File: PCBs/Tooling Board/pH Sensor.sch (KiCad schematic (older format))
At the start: 28 parts

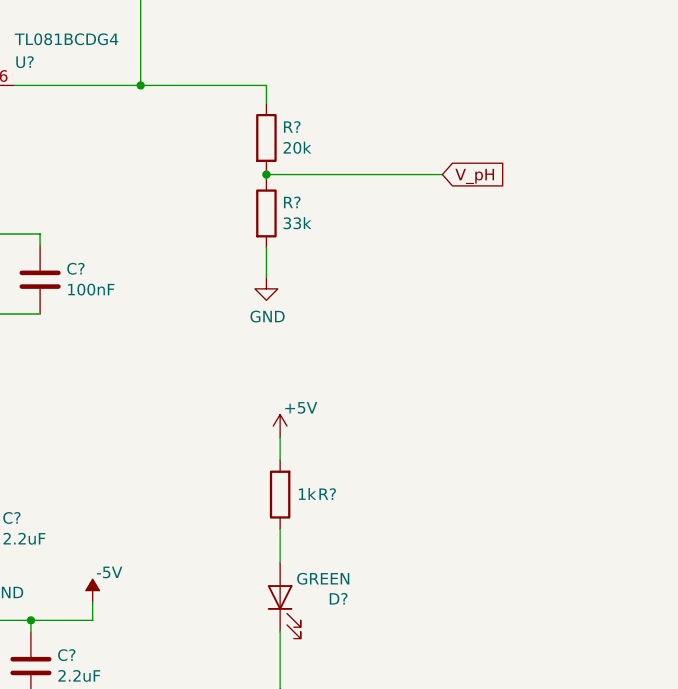
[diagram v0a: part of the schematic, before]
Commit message: Pins are Mapped
-This was really difficult and it may not work.
-We're gonna try it and see what works.
-If it fails the next PCB will use arduino atmega chips since the open source libraries exist for them
-Might do a combination of SAMD and atmega lol
-God damn chinese new year
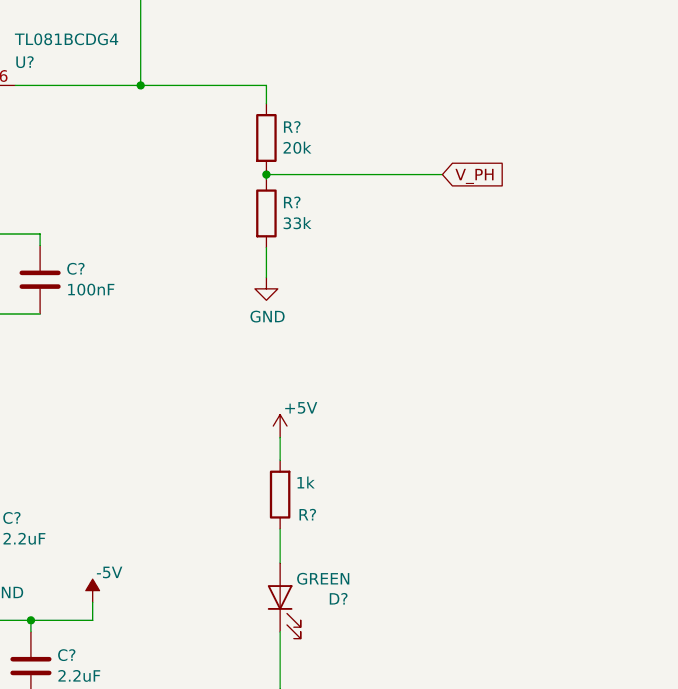
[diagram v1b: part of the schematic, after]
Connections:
- net V_pH renamed V_PH
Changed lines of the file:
@@
 EESchema Schematic File Version 4
-LIBS:Actuator Board-cache
+LIBS:Tooling Board-cache
 EELAYER 26 0
 EELAYER END
@@
 U 1 1 5BE3019B
 P 8510 4190
-F 0 "R?" H 8303 4190 50  0000 C CNN
-F 1 "1k" H 8394 4190 50  0000 C CNN
+F 0 "R?" H 8390 4280 50  0000 C CNN
+F 1 "1k" H 8400 4140 50  0000 C CNN
 F 2 "" V 8440 4190 50  0001 C CNN
 F 3 "~" H 8510 4190 50  0001 C CNN
@@
 	5980 1490 5980 1550
 Text GLabel 9220 2790 2    50   Input ~ 0
-V_pH
-$Comp
-L Device:R R?
+V_PH
+$Comp
+L Device:R R?

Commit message: Added Footprints
-Whoooo boy here we go
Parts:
- C801, C802, C803, C804, C805, C806, C807, C808, C809, C810, C811, C812, C813: renamed from C?; footprint (none) -> Capacitors_SMD:C_0805_HandSoldering
- D801: renamed from D?; footprint (none) -> LEDs:LED_0805_HandSoldering
- J801: renamed from J?; footprint (none) -> Junction Box:70553-02
- R801, R802, R803, R804, R805, R806, R807, R808, R809: renamed from R?; footprint (none) -> Resistors_SMD:R_0805_HandSoldering
- RV801: renamed from RV?; footprint (none) -> Potentiometers:Potentiometer_Trimmer_Bourns_3269W
- U801, U803: renamed from U?; footprint (none) -> SMD_Packages:SOIC-8-N
- U802: renamed from U?; footprint Package_TO_SOT_SMD:SOT-23-6 -> TO_SOT_Packages_SMD:SOT-23-6

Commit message: Almost Finished
-Still going, help
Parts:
- removed D801: GREEN, LEDs:LED_0805_HandSoldering, symbol Device:LED
- removed R809: 1k, Resistors_SMD:R_0805_HandSoldering, symbol Device:R
- C801, C802, C803, C804, C805, C806, C807, C808, C809, C810, C811, C812, C813: footprint Capacitors_SMD:C_0805_HandSoldering -> Capacitors_SMD:C_0805
- J801: footprint Junction Box:70553-02 -> EER:1x2_molex_llc_new
- R801, R802, R803, R804, R805, R806, R807, R808: footprint Resistors_SMD:R_0805_HandSoldering -> Resistors_SMD:R_0805
- RV801: footprint Potentiometers:Potentiometer_Trimmer_Bourns_3269W -> Potentiometers:Potentiometer_Trimmer_Bourns_3296W
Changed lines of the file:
@@
 $Descr A4 11693 8268
 encoding utf-8
-Sheet 8 7
+Sheet 7 7
 Title ""
 Date ""
@@
 F 0 "R801" V 1953 2400 50  0000 C CNN
 F 1 "4.7M" V 2044 2400 50  0000 C CNN
-F 2 "Resistors_SMD:R_0805_HandSoldering" V 2090 2400 50  0001 C CNN
+F 2 "Resistors_SMD:R_0805" V 2090 2400 50  0001 C CNN
 F 3 "~" H 2160 2400 50  0001 C CNN
 	1    2160 2400
@@
 F 0 "C802" H 2615 2746 50  0000 L CNN
 F 1 "2.2nF" H 2615 2655 50  0000 L CNN
-F 2 "Capacitors_SMD:C_0805_HandSoldering" H 2538 2550 50  0001 C CNN
+F 2 "Capacitors_SMD:C_0805" H 2538 2550 50  0001 C CNN
 F 3 "~" H 2500 2700 50  0001 C CNN
 	1    2500 2700
@@
 F 0 "C801" H 2415 3546 50  0000 L CNN
 F 1 "10uF" H 2415 3455 50  0000 L CNN
-F 2 "Capacitors_SMD:C_0805_HandSoldering" H 2338 3350 50  0001 C CNN
+F 2 "Capacitors_SMD:C_0805" H 2338 3350 50  0001 C CNN
 F 3 "~" H 2300 3500 50  0001 C CNN
 	1    2300 3500
@@
 F 0 "C803" H 2965 3546 50  0000 L CNN
 F 1 "100nF" H 2965 3455 50  0000 L CNN
-F 2 "Capacitors_SMD:C_0805_HandSoldering" H 2888 3350 50  0001 C CNN
+F 2 "Capacitors_SMD:C_0805" H 2888 3350 50  0001 C CNN
 F 3 "~" H 2850 3500 50  0001 C CNN
 	1    2850 3500
@@
 F 0 "C806" V 3598 3550 50  0000 C CNN
 F 1 "1uF" V 3689 3550 50  0000 C CNN
-F 2 "Capacitors_SMD:C_0805_HandSoldering" H 3888 3400 50  0001 C CNN
+F 2 "Capacitors_SMD:C_0805" H 3888 3400 50  0001 C CNN
 F 3 "~" H 3850 3550 50  0001 C CNN
 	1    3850 3550
@@
 F 0 "R803" H 4570 3916 50  0000 L CNN
 F 1 "2.2k" H 4570 3825 50  0000 L CNN
-F 2 "Resistors_SMD:R_0805_HandSoldering" V 4430 3870 50  0001 C CNN
+F 2 "Resistors_SMD:R_0805" V 4430 3870 50  0001 C CNN
 F 3 "~" H 4500 3870 50  0001 C CNN
 	1    4500 3870
@@
 F 0 "R802" V 3943 4850 50  0000 C CNN
 F 1 "1k" V 4034 4850 50  0000 C CNN
-F 2 "Resistors_SMD:R_0805_HandSoldering" V 4080 4850 50  0001 C CNN
+F 2 "Resistors_SMD:R_0805" V 4080 4850 50  0001 C CNN
 F 3 "~" H 4150 4850 50  0001 C CNN
 	1    4150 4850
@@
 F 0 "C805" H 3665 1846 50  0000 L CNN
 F 1 "10uF" H 3665 1755 50  0000 L CNN
-F 2 "Capacitors_SMD:C_0805_HandSoldering" H 3588 1650 50  0001 C CNN
+F 2 "Capacitors_SMD:C_0805" H 3588 1650 50  0001 C CNN
 F 3 "~" H 3550 1800 50  0001 C CNN
 	1    3550 1800
@@
 	4500 2500 3950 2500
 Connection ~ 3250 3550
-Connection ~ 4500 3550
 Wire Wire Line
 	4500 3550 4500 2500
@@
 F 0 "R804" V 5643 2500 50  0000 C CNN
 F 1 "30k" V 5734 2500 50  0000 C CNN
-F 2 "Resistors_SMD:R_0805_HandSoldering" V 5780 2500 50  0001 C CNN
+F 2 "Resistors_SMD:R_0805" V 5780 2500 50  0001 C CNN
 F 3 "~" H 5850 2500 50  0001 C CNN
 	1    5850 2500
@@
 F 0 "C807" H 5615 1766 50  0000 L CNN
 F 1 "10uF" H 5615 1675 50  0000 L CNN
-F 2 "Capacitors_SMD:C_0805_HandSoldering" H 5538 1570 50  0001 C CNN
+F 2 "Capacitors_SMD:C_0805" H 5538 1570 50  0001 C CNN
 F 3 "~" H 5500 1720 50  0001 C CNN
 	1    5500 1720
@@
 F 0 "C809" H 6095 1796 50  0000 L CNN
 F 1 "100nF" H 6095 1705 50  0000 L CNN
-F 2 "Capacitors_SMD:C_0805_HandSoldering" H 6018 1600 50  0001 C CNN
+F 2 "Capacitors_SMD:C_0805" H 6018 1600 50  0001 C CNN
 F 3 "~" H 5980 1750 50  0001 C CNN
 	1    5980 1750
@@
 F 0 "R806" V 7093 1450 50  0000 C CNN
 F 1 "30k" V 7184 1450 50  0000 C CNN
-F 2 "Resistors_SMD:R_0805_HandSoldering" V 7230 1450 50  0001 C CNN
+F 2 "Resistors_SMD:R_0805" V 7230 1450 50  0001 C CNN
 F 3 "~" H 7300 1450 50  0001 C CNN
 	1    7300 1450
@@
 F 0 "R805" H 6420 2956 50  0000 L CNN
 F 1 "75k" H 6420 2865 50  0000 L CNN
-F 2 "Resistors_SMD:R_0805_HandSoldering" V 6280 2910 50  0001 C CNN
+F 2 "Resistors_SMD:R_0805" V 6280 2910 50  0001 C CNN
 F 3 "~" H 6350 2910 50  0001 C CNN
 	1    6350 2910
@@
 F 0 "C810" H 7065 3296 50  0000 L CNN
 F 1 "10uF" H 7065 3205 50  0000 L CNN
-F 2 "Capacitors_SMD:C_0805_HandSoldering" H 6988 3100 50  0001 C CNN
+F 2 "Capacitors_SMD:C_0805" H 6988 3100 50  0001 C CNN
 F 3 "~" H 6950 3250 50  0001 C CNN
 	1    6950 3250
@@
 F 0 "C813" H 7575 3296 50  0000 L CNN
 F 1 "100nF" H 7575 3205 50  0000 L CNN
-F 2 "Capacitors_SMD:C_0805_HandSoldering" H 7498 3100 50  0001 C CNN
+F 2 "Capacitors_SMD:C_0805" H 7498 3100 50  0001 C CNN
 F 3 "~" H 7460 3250 50  0001 C CNN
 	1    7460 3250
@@
 Text Notes 5540 4400 0    50   ~ 0
 Converts the +5 to -5 volts
-$Comp
-L power:+5V #PWR0185
-U 1 1 5BE2F1EF
-P 8510 3940
-F 0 "#PWR0185" H 8510 3790 50  0001 C CNN
-F 1 "+5V" H 8525 4068 50  0000 L CNN
-F 2 "" H 8510 3940 50  0001 C CNN
-F 3 "" H 8510 3940 50  0001 C CNN
-	1    8510 3940
-	1    0    0    -1
-$EndComp
-Wire Wire Line
-	8510 3940 8510 4040
-$Comp
-L Device:R R809
-U 1 1 5BE3019B
-P 8510 4190
-F 0 "R809" H 8390 4280 50  0000 C CNN
-F 1 "1k" H 8400 4140 50  0000 C CNN
-F 2 "Resistors_SMD:R_0805_HandSoldering" V 8440 4190 50  0001 C CNN
-F 3 "~" H 8510 4190 50  0001 C CNN
-	1    8510 4190
-	-1   0    0    1
-$EndComp
-Wire Wire Line
-	8510 4340 8510 4490
-$Comp
-L Device:LED D801
-U 1 1 5BE3119A
-P 8510 4640
-F 0 "D801" V 8502 4385 50  0000 C CNN
-F 1 "GREEN" V 8590 4450 50  0000 C CNN
-F 2 "LEDs:LED_0805_HandSoldering" H 8510 4640 50  0001 C CNN
-F 3 "~" H 8510 4640 50  0001 C CNN
-	1    8510 4640
-	0    -1   -1   0
-$EndComp
-Wire Wire Line
-	8510 4790 8510 5040
-$Comp
-L power:GND #PWR0186
-U 1 1 5BE3223A
-P 8510 5040
-F 0 "#PWR0186" H 8510 4790 50  0001 C CNN
-F 1 "GND" H 8580 4900 50  0000 R CNN
-F 2 "" H 8510 5040 50  0001 C CNN
-F 3 "" H 8510 5040 50  0001 C CNN
-	1    8510 5040
-	1    0    0    -1
-$EndComp
 Wire Wire Line
 	3250 2600 3250 3550
@@
 F 0 "J801" H 1430 2175 50  0000 C CNN
 F 1 "Conn_01x02" H 1430 2266 50  0000 C CNN
-F 2 "Junction Box:70553-02" H 1510 2500 50  0001 C CNN
+F 2 "EER:1x2_molex_llc_new" H 1510 2500 50  0001 C CNN
 F 3 "~" H 1510 2500 50  0001 C CNN
 	1    1510 2500
@@
 F 0 "C804" H 3115 1846 50  0000 L CNN
 F 1 "100nF" H 3115 1755 50  0000 L CNN
-F 2 "Capacitors_SMD:C_0805_HandSoldering" H 3038 1650 50  0001 C CNN
+F 2 "Capacitors_SMD:C_0805" H 3038 1650 50  0001 C CNN
 F 3 "~" H 3000 1800 50  0001 C CNN
 	1    3000 1800
@@
 F 0 "RV801" H 4433 4404 50  0000 R CNN
 F 1 "5k" H 4433 4495 50  0000 R CNN
-F 2 "Potentiometers:Potentiometer_Trimmer_Bourns_3269W" H 4500 4450 50  0001 C CNN
+F 2 "Potentiometers:Potentiometer_Trimmer_Bourns_3296W" H 4500 4450 50  0001 C CNN
 F 3 "https://www.digikey.ca/product-detail/en/bourns-inc/3296W-1-502LF/3296W-502LF-ND/1088058" H 4500 4450 50  0001 C CNN
 	1    4500 4450
@@
 F 0 "R808" H 8520 3006 50  0000 L CNN
 F 1 "33k" H 8520 2915 50  0000 L CNN
-F 2 "Resistors_SMD:R_0805_HandSoldering" V 8380 2960 50  0001 C CNN
+F 2 "Resistors_SMD:R_0805" V 8380 2960 50  0001 C CNN
 F 3 "~" H 8450 2960 50  0001 C CNN
 	1    8450 2960
@@
 F 0 "R807" H 8520 2676 50  0000 L CNN
 F 1 "20k" H 8520 2585 50  0000 L CNN
-F 2 "Resistors_SMD:R_0805_HandSoldering" V 8380 2630 50  0001 C CNN
+F 2 "Resistors_SMD:R_0805" V 8380 2630 50  0001 C CNN
 F 3 "~" H 8450 2630 50  0001 C CNN
 	1    8450 2630
@@
 F 0 "C811" H 7295 4386 50  0000 L CNN
 F 1 "2.2uF" H 7295 4295 50  0000 L CNN
-F 2 "Capacitors_SMD:C_0805_HandSoldering" H 7218 4190 50  0001 C CNN
+F 2 "Capacitors_SMD:C_0805" H 7218 4190 50  0001 C CNN
 F 3 "~" H 7180 4340 50  0001 C CNN
 	1    7180 4340
@@
 F 0 "C812" H 7535 4986 50  0000 L CNN
 F 1 "2.2uF" H 7535 4895 50  0000 L CNN
-F 2 "Capacitors_SMD:C_0805_HandSoldering" H 7458 4790 50  0001 C CNN
+F 2 "Capacitors_SMD:C_0805" H 7458 4790 50  0001 C CNN
 F 3 "~" H 7420 4940 50  0001 C CNN
 	1    7420 4940
@@
 F 0 "C808" H 6045 5036 50  0000 L CNN
 F 1 "2.2uF" H 6045 4945 50  0000 L CNN
-F 2 "Capacitors_SMD:C_0805_HandSoldering" H 5968 4840 50  0001 C CNN
+F 2 "Capacitors_SMD:C_0805" H 5968 4840 50  0001 C CNN
 F 3 "~" H 5930 4990 50  0001 C CNN
 	1    5930 4990

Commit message: tooling board bom
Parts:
- C801, C805, C807, C810: Digikey (none) -> 1276-2872-1-ND
- C802, C808, C811, C812: Digikey (none) -> 587-1293-1-ND
- C803, C804, C809, C813: Digikey (none) -> 311-1140-1-ND
- C806: Digikey (none) -> 1276-6470-1-ND
- J801: Digikey (none) -> WM4800-ND
- R801: Digikey (none) -> RMCF0805FT4M70CT-ND
- R802: Digikey (none) -> RR12P1.0KDCT-ND
- R803: Digikey (none) -> 311-2.20KCRCT-ND
- R804, R806: Digikey (none) -> A126360CT-ND
- R805: Digikey (none) -> YAG3750CT-ND
- R807: Digikey (none) -> A126349CT-ND
- R808: Digikey (none) -> RR12P33.0KDCT-ND
- RV801: Digikey (none) -> 490-2888-ND
- U801: Digikey (none) -> CA3140AMZ-ND
- U802: Digikey (none) -> 296-43957-1-ND
- U803: Digikey (none) -> 296-34259-5-ND
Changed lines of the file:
@@
 F 2 "Resistors_SMD:R_0805" V 2090 2400 50  0001 C CNN
 F 3 "~" H 2160 2400 50  0001 C CNN
+F 4 "RMCF0805FT4M70CT-ND" V 2160 2400 50  0001 C CNN "Digikey"
 	1    2160 2400
 	0    1    1    0
@@
 F 2 "Capacitors_SMD:C_0805" H 2538 2550 50  0001 C CNN
 F 3 "~" H 2500 2700 50  0001 C CNN
+F 4 "587-1293-1-ND" H 2500 2700 50  0001 C CNN "Digikey"
 	1    2500 2700
 	1    0    0    -1
@@
 F 2 "Capacitors_SMD:C_0805" H 2338 3350 50  0001 C CNN
 F 3 "~" H 2300 3500 50  0001 C CNN
+F 4 "1276-2872-1-ND" H 2300 3500 50  0001 C CNN "Digikey"
 	1    2300 3500
 	1    0    0    -1
@@
 F 2 "Capacitors_SMD:C_0805" H 2888 3350 50  0001 C CNN
 F 3 "~" H 2850 3500 50  0001 C CNN
+F 4 "311-1140-1-ND" H 2850 3500 50  0001 C CNN "Digikey"
 	1    2850 3500
 	1    0    0    -1
@@
 F 2 "Capacitors_SMD:C_0805" H 3888 3400 50  0001 C CNN
 F 3 "~" H 3850 3550 50  0001 C CNN
+F 4 "1276-6470-1-ND" V 3850 3550 50  0001 C CNN "Digikey"
 	1    3850 3550
 	0    1    1    0
@@
 F 2 "Resistors_SMD:R_0805" V 4430 3870 50  0001 C CNN
 F 3 "~" H 4500 3870 50  0001 C CNN
+F 4 "311-2.20KCRCT-ND" H 4500 3870 50  0001 C CNN "Digikey"
 	1    4500 3870
 	1    0    0    -1
@@
 F 2 "Resistors_SMD:R_0805" V 4080 4850 50  0001 C CNN
 F 3 "~" H 4150 4850 50  0001 C CNN
+F 4 "RR12P1.0KDCT-ND" V 4150 4850 50  0001 C CNN "Digikey"
 	1    4150 4850
 	0    1    1    0
@@
 F 2 "Capacitors_SMD:C_0805" H 3588 1650 50  0001 C CNN
 F 3 "~" H 3550 1800 50  0001 C CNN
+F 4 "1276-2872-1-ND" H 3550 1800 50  0001 C CNN "Digikey"
 	1    3550 1800
 	1    0    0    -1
@@
 F 2 "Resistors_SMD:R_0805" V 5780 2500 50  0001 C CNN
 F 3 "~" H 5850 2500 50  0001 C CNN
+F 4 "A126360CT-ND" V 5850 2500 50  0001 C CNN "Digikey"
 	1    5850 2500
 	0    1    1    0
@@
 F 2 "Capacitors_SMD:C_0805" H 5538 1570 50  0001 C CNN
 F 3 "~" H 5500 1720 50  0001 C CNN
+F 4 "1276-2872-1-ND" H 5500 1720 50  0001 C CNN "Digikey"
 	1    5500 1720
 	1    0    0    -1
@@
 F 2 "Capacitors_SMD:C_0805" H 6018 1600 50  0001 C CNN
 F 3 "~" H 5980 1750 50  0001 C CNN
+F 4 "311-1140-1-ND" H 5980 1750 50  0001 C CNN "Digikey"
 	1    5980 1750
 	1    0    0    -1
@@
 F 2 "Resistors_SMD:R_0805" V 7230 1450 50  0001 C CNN
 F 3 "~" H 7300 1450 50  0001 C CNN
+F 4 "A126360CT-ND" V 7300 1450 50  0001 C CNN "Digikey"
 	1    7300 1450
 	0    1    1    0
@@
 F 2 "Resistors_SMD:R_0805" V 6280 2910 50  0001 C CNN
 F 3 "~" H 6350 2910 50  0001 C CNN
+F 4 "YAG3750CT-ND" H 6350 2910 50  0001 C CNN "Digikey"
 	1    6350 2910
 	1    0    0    -1
@@
 F 2 "Capacitors_SMD:C_0805" H 6988 3100 50  0001 C CNN
 F 3 "~" H 6950 3250 50  0001 C CNN
+F 4 "1276-2872-1-ND" H 6950 3250 50  0001 C CNN "Digikey"
 	1    6950 3250
 	1    0    0    -1
@@
 F 2 "Capacitors_SMD:C_0805" H 7498 3100 50  0001 C CNN
 F 3 "~" H 7460 3250 50  0001 C CNN
+F 4 "311-1140-1-ND" H 7460 3250 50  0001 C CNN "Digikey"
 	1    7460 3250
 	1    0    0    -1
@@
 F 2 "EER:1x2_molex_llc_new" H 1510 2500 50  0001 C CNN
 F 3 "~" H 1510 2500 50  0001 C CNN
+F 4 "WM4800-ND" H 1510 2500 50  0001 C CNN "Digikey"
 	1    1510 2500
 	-1   0    0    1
@@
 F 2 "Capacitors_SMD:C_0805" H 3038 1650 50  0001 C CNN
 F 3 "~" H 3000 1800 50  0001 C CNN
+F 4 "311-1140-1-ND" H 3000 1800 50  0001 C CNN "Digikey"
 	1    3000 1800
 	1    0    0    -1
@@
 F 2 "Potentiometers:Potentiometer_Trimmer_Bourns_3296W" H 4500 4450 50  0001 C CNN
 F 3 "https://www.digikey.ca/product-detail/en/bourns-inc/3296W-1-502LF/3296W-502LF-ND/1088058" H 4500 4450 50  0001 C CNN
+F 4 "490-2888-ND" H 4500 4450 50  0001 C CNN "Digikey"
 	1    4500 4450
 	-1   0    0    1
@@
 F 2 "Resistors_SMD:R_0805" V 8380 2960 50  0001 C CNN
 F 3 "~" H 8450 2960 50  0001 C CNN
+F 4 "RR12P33.0KDCT-ND" H 8450 2960 50  0001 C CNN "Digikey"
 	1    8450 2960
 	1    0    0    -1
@@
 F 2 "Resistors_SMD:R_0805" V 8380 2630 50  0001 C CNN
 F 3 "~" H 8450 2630 50  0001 C CNN
+F 4 "A126349CT-ND" H 8450 2630 50  0001 C CNN "Digikey"
 	1    8450 2630
 	1    0    0    -1
@@
 F 2 "SMD_Packages:SOIC-8-N" H 6950 2300 50  0001 C CNN
 F 3 "https://www.digikey.ca/products/en?keywords=TL081BCDG4" H 7050 2400 50  0001 C CNN
+F 4 "296-34259-5-ND" H 7050 2400 50  0001 C CNN "Digikey"
 	1    7050 2400
 	1    0    0    -1
@@
 F 2 "SMD_Packages:SOIC-8-N" H 3550 2400 50  0001 C CNN
 F 3 "https://www.digikey.ca/product-detail/en/renesas-electronics-america-inc/CA3140AMZ/CA3140AMZ-ND/821387" H 3650 2500 50  0001 C CNN
+F 4 "CA3140AMZ-ND" H 3650 2500 50  0001 C CNN "Digikey"
 	1    3650 2500
 	1    0    0    -1
@@
 F 2 "TO_SOT_Packages_SMD:SOT-23-6" H 6840 4490 50  0001 L CNN
 F 3 "https://www.digikey.ca/product-detail/en/texas-instruments/LM2776DBVR/296-43957-1-ND/5973203" H 4940 6090 50  0001 C CNN
+F 4 "296-43957-1-ND" H 6790 4840 50  0001 C CNN "Digikey"
 	1    6790 4840
 	1    0    0    -1
@@
 F 2 "Capacitors_SMD:C_0805" H 7218 4190 50  0001 C CNN
 F 3 "~" H 7180 4340 50  0001 C CNN
+F 4 "587-1293-1-ND" H 7180 4340 50  0001 C CNN "Digikey"
 	1    7180 4340
 	1    0    0    -1
@@
 F 2 "Capacitors_SMD:C_0805" H 7458 4790 50  0001 C CNN
 F 3 "~" H 7420 4940 50  0001 C CNN
+F 4 "587-1293-1-ND" H 7420 4940 50  0001 C CNN "Digikey"
 	1    7420 4940
 	1    0    0    -1
@@
 F 2 "Capacitors_SMD:C_0805" H 5968 4840 50  0001 C CNN
 F 3 "~" H 5930 4990 50  0001 C CNN
+F 4 "587-1293-1-ND" H 5930 4990 50  0001 C CNN "Digikey"
 	1    5930 4990
 	1    0    0    -1
